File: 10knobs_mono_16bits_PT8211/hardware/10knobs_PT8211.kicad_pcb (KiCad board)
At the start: 2 copper layers, 47 parts, among them J1 Conn_01x06_Female, U1 PT8211, U2 BluePill_STM32F103C, U3 6N138, U4 LM358

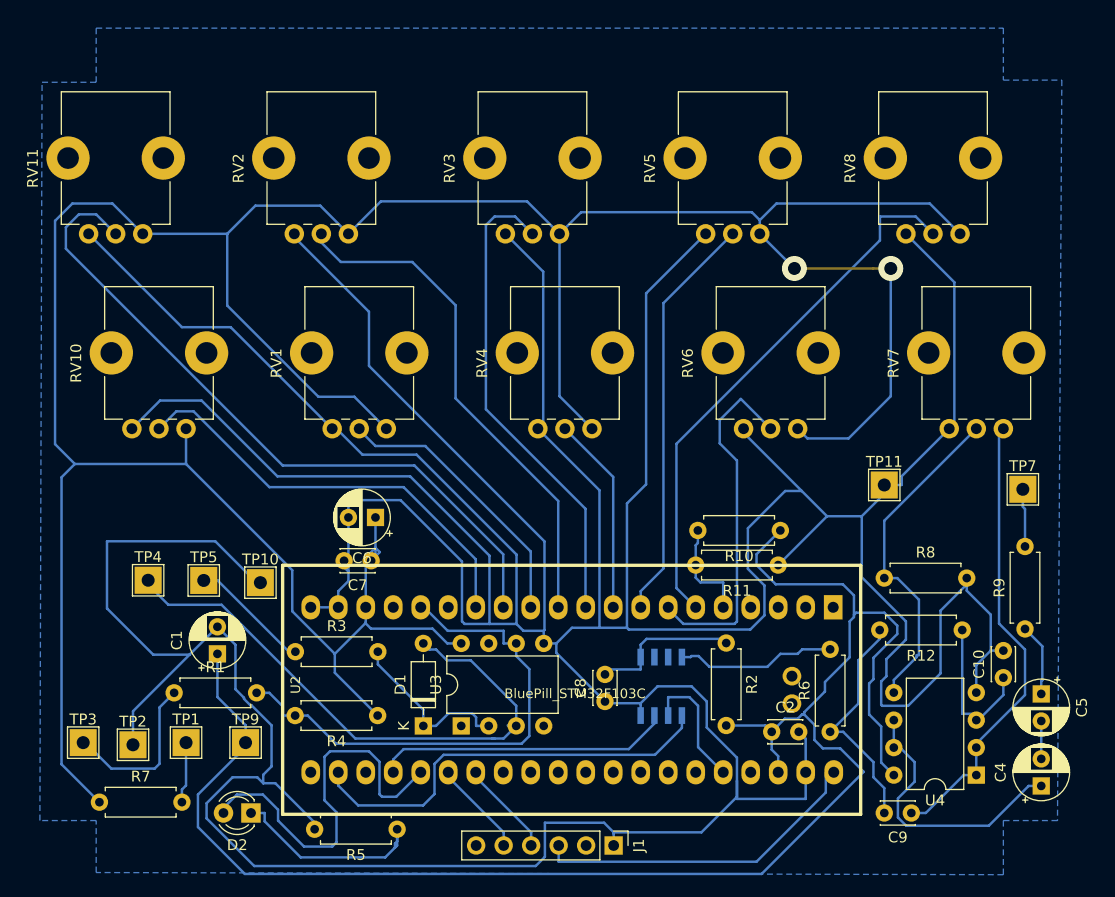
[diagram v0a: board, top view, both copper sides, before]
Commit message: Added a stab capacitor on the DAC
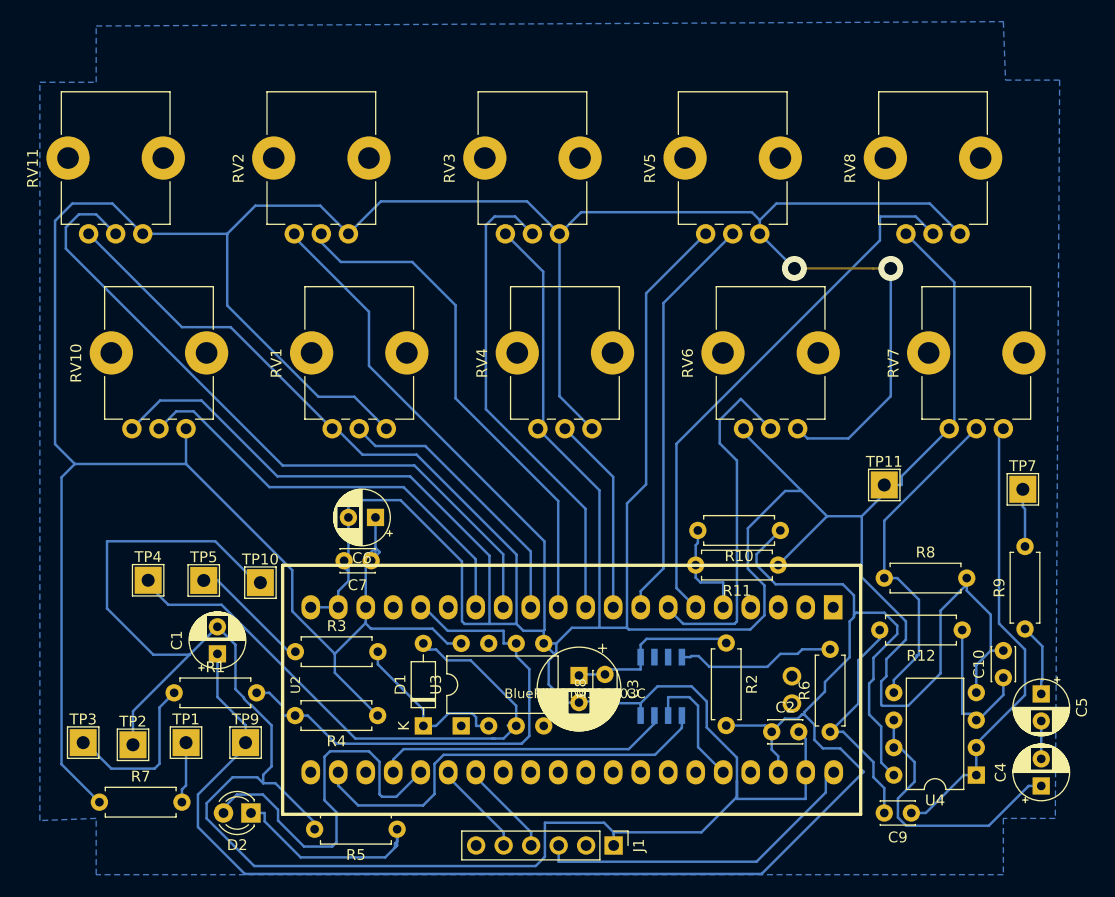
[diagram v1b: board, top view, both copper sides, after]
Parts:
- added C3: 1000uF, Capacitor_THT:CP_Radial_D7.5mm_P2.50mm, F.Cu at (95.8, 79.8)
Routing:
- net GND: track 590.1 -> 594.4 mm
- net Net-(C3-Pad1): track 14.1 -> 16.5 mm
